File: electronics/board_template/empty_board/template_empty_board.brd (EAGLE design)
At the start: 48 x 48 mm, 8 parts, among them IC1 L7805CD2T-TR, J1 GROVE_CONNECTOR2.0_1X4, J2 GROVE_CONNECTOR2.0_1X4

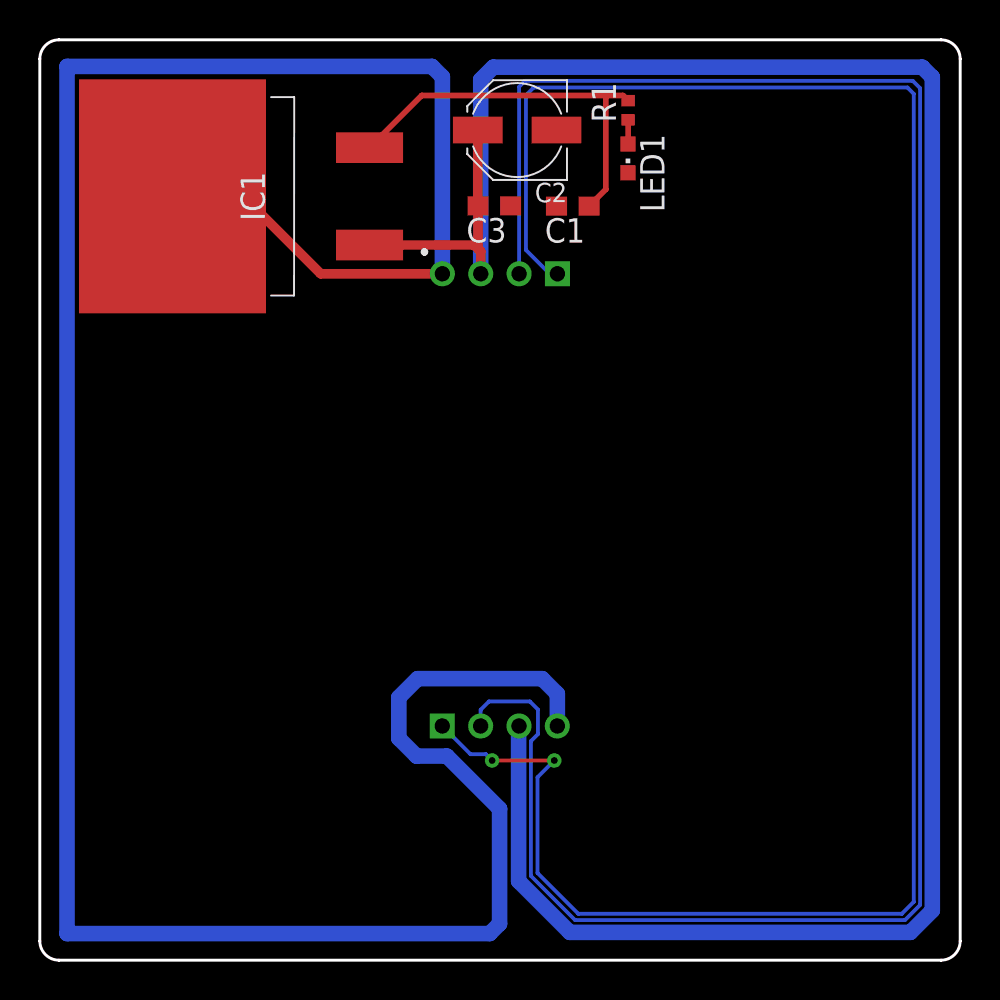
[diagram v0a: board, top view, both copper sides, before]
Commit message: Template Empty Board an anderen Linearregler angepasst
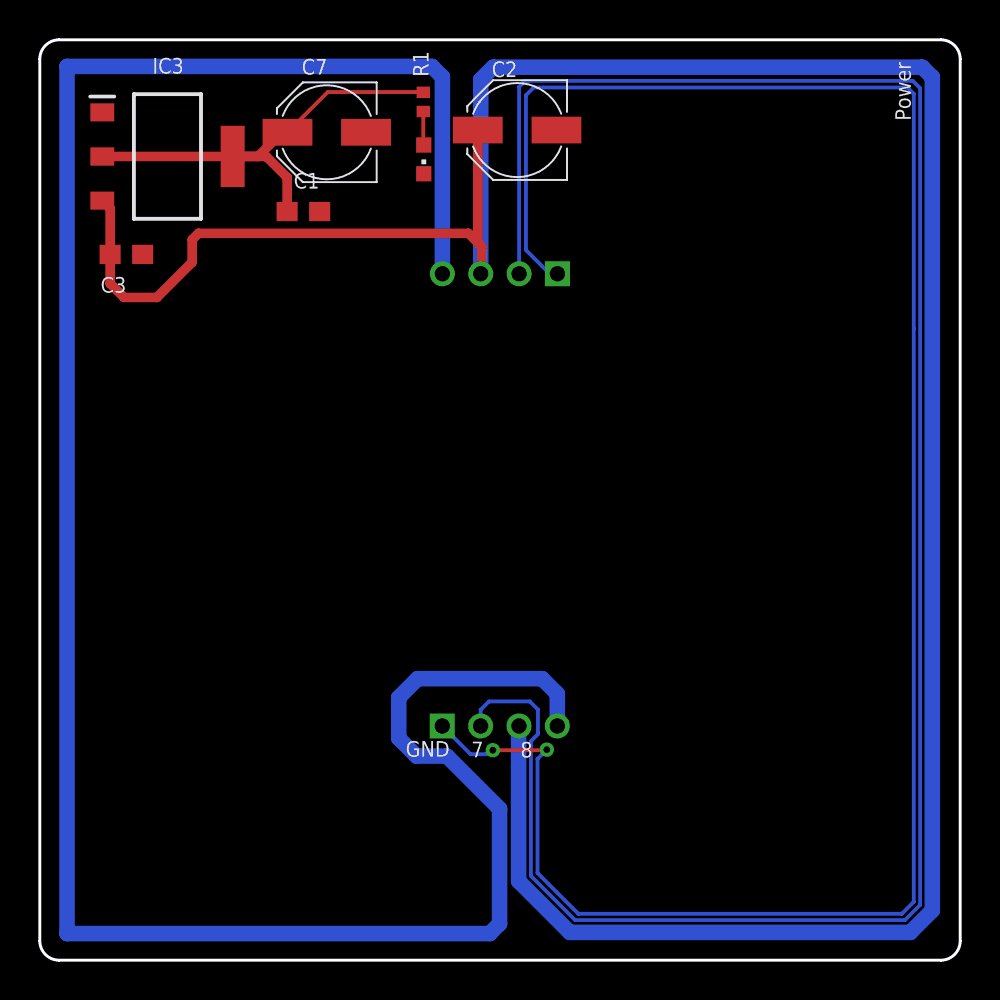
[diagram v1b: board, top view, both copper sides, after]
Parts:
- removed IC1: L7805CD2T-TR, morphbot:L7805CD2T
- added C7: ST(Semtech) CK1C470M-CRD54 - 47uF, rcl:PANASONIC_C
- added IC3: NCP1117ST50T3G, samacsys:SOT230P700X180-4N@1
- moved C3 19.4 mm to (4.52, 36.8)
- moved C1 14.1 mm to (13.7, 39.0), turned to 0 degrees
- moved R1 10.7 mm to (20.0, 44.8)
- moved LED1 10.6 mm to (20.0, 41.8)
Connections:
- net SCL renamed PC5/SCL
- net SDA renamed PC4/SDA
- net +5V: now also C7.+, IC3.2, IC3.4; no longer IC1.3
- net GND: now also C7.-, IC3.1; no longer IC1.2
- net VCC: now also IC3.3; no longer IC1.1
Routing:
- net VCC: track 122.4 -> 143.0 mm
- net GND: track 139.4 -> 124.3 mm
- net +5V: track 20.9 -> 23.9 mm
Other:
- board text added: "7"
- board text added: "8"
- board text added: "GND"
- board text added: "Power"

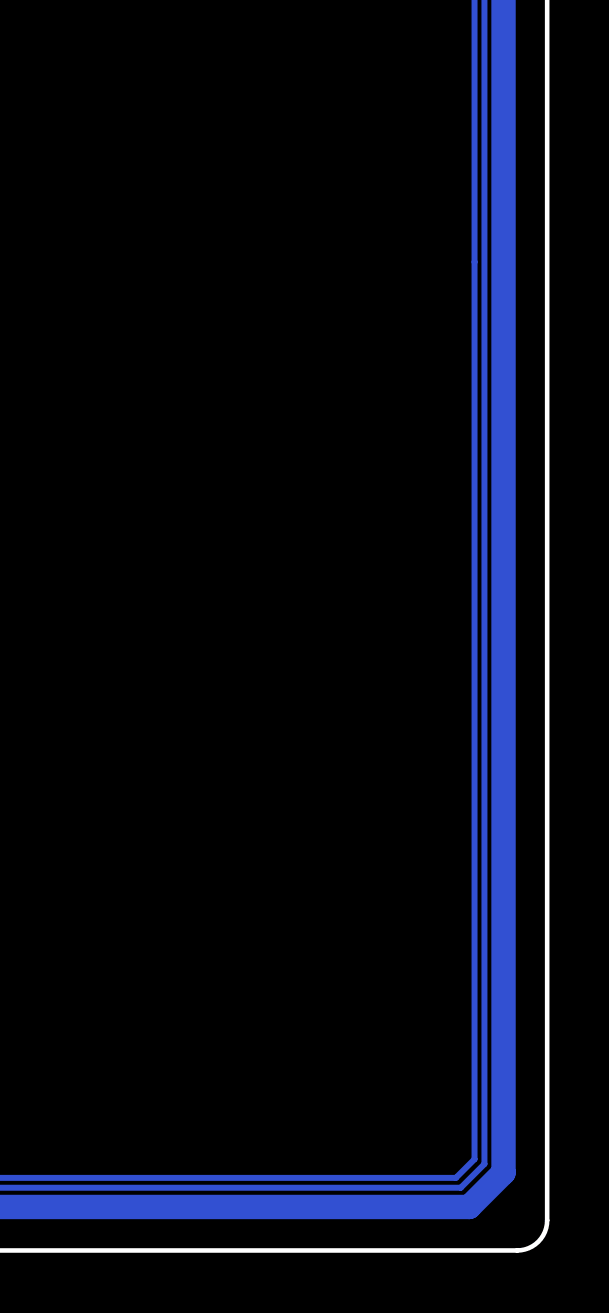
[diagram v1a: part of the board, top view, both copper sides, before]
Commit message: Logo hinzugefügt
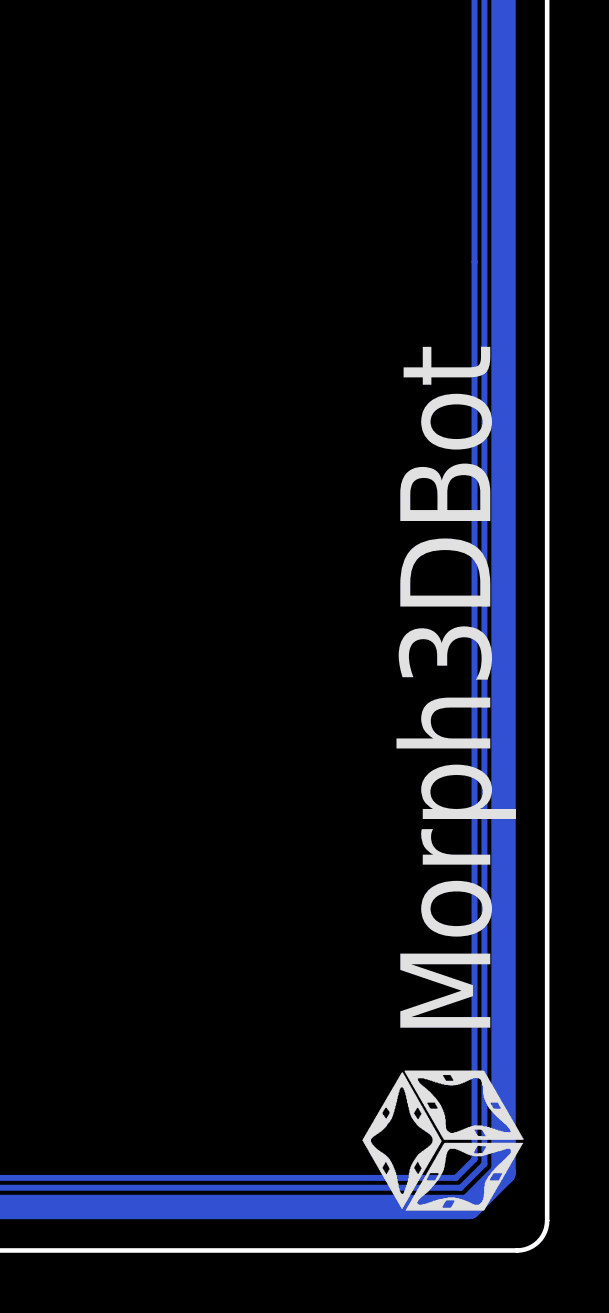
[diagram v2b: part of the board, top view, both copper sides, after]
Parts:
- added U$1: LOGO_MORPHBOT5MM, topo-eng:LOGO_MORPHBOT
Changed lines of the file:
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@@
 <layer number="104" name="Name" color="7" fill="1" visible="no" active="yes"/>
 <layer number="116" name="Patch_BOT" color="9" fill="4" visible="no" active="yes"/>
+<layer number="120" name="brd_placement_notes" color="7" fill="1" visible="yes" active="yes"/>
 <layer number="121" name="_tsilk" color="7" fill="1" visible="no" active="yes"/>
 <layer number="122" name="_bsilk" color="7" fill="1" visible="no" active="yes"/>
+<layer number="144" name="DrillLegend" color="7" fill="1" visible="yes" active="yes"/>
+<layer number="145" name="DrillLegend_01-16" color="7" fill="1" visible="yes" active="yes"/>
+<layer number="146" name="DrillLegend_01-20" color="7" fill="1" visible="yes" active="yes"/>
 <layer number="151" name="HeatSink" color="14" fill="1" visible="no" active="no"/>
+<layer number="198" name="BMP198" color="7" fill="1" visible="yes" active="yes"/>
+<layer number="199" name="Contour" color="7" fill="1" visible="yes" active="yes"/>
 <layer number="200" name="200bmp" color="1" fill="10" visible="no" active="no"/>
 <layer number="201" name="201bmp" color="2" fill="1" visible="no" active="no"/>
@@
 <layer number="207" name="207bmp" color="15" fill="10" visible="no" active="no"/>
 <layer number="208" name="208bmp" color="9" fill="10" visible="no" active="yes"/>
+<layer number="209" name="Route9Document" color="7" fill="1" visible="yes" active="yes"/>
+<layer number="210" name="Route10Document" color="7" fill="1" visible="yes" active="yes"/>
+<layer number="211" name="Route11Document" color="7" fill="1" visible="yes" active="yes"/>
+<layer number="212" name="Route12Document" color="7" fill="1" visible="yes" active="yes"/>
+<layer number="213" name="Route13Document" color="7" fill="1" visible="yes" active="yes"/>
+<layer number="214" name="Route14Document" color="7" fill="1" visible="yes" active="yes"/>
+<layer number="215" name="Route15Document" color="7" fill="1" visible="yes" active="yes"/>
+<layer number="216" name="BottomDocument" color="7" fill="1" visible="yes" active="yes"/>
+<layer number="220" name="DimensionDocument" color="7" fill="1" visible="yes" active="yes"/>
+<layer number="221" name="tPlaceDocument" color="7" fill="1" visible="yes" active="yes"/>
+<layer number="222" name="bPlaceDocument" color="7" fill="1" visible="yes" active="yes"/>
+<layer number="225" name="tNamesDocument" color="7" fill="1" visible="yes" active="yes"/>
+<layer number="226" name="bNamesDocument" color="7" fill="1" visible="yes" active="yes"/>
+<layer number="227" name="tValuesDocument" color="7" fill="1" visible="yes" active="yes"/>
+<layer number="228" name="bValuesDocument" color="7" fill="1" visible="yes" active="yes"/>
+<layer number="229" name="tStopDocument" color="7" fill="1" visible="yes" active="yes"/>
+<layer number="230" name="bStopDocument" color="7" fill="1" visible="yes" active="yes"/>
+<layer number="231" name="tCreamDocument" color="7" fill="1" visible="yes" active="yes"/>
+<layer number="232" name="bCreamDocument" color="7" fill="1" visible="yes" active="yes"/>
+<layer number="233" name="tFinishDocument" color="7" fill="1" visible="yes" active="yes"/>
+<layer number="234" name="bFinishDocument" color="7" fill="1" visible="yes" active="yes"/>
+<layer number="235" name="tGlueDocument" color="7" fill="1" visible="yes" active="yes"/>
+<layer number="236" name="bGlueDocument" color="7" fill="1" visible="yes" active="yes"/>
+<layer number="244" name="DrillsDocument" color="7" fill="1" visible="yes" active="yes"/>
+<layer number="245" name="HolesDocument" color="7" fill="1" visible="yes" active="yes"/>
+<layer number="246" name="MillingDocument" color="7" fill="1" visible="yes" active="yes"/>
+<layer number="247" name="MeasuresDocument" color="7" fill="1" visible="yes" active="yes"/>
 <layer number="250" name="Descript" color="3" fill="1" visible="no" active="no"/>
 <layer number="251" name="SMDround" color="12" fill="11" visible="no" active="no"/>
@@
 <attribute name="VALUE" x="17.61630625" y="46.952225" size="1.016" layer="27" rot="R180"/>
 </element>
+<element name="U$1" library="topo-eng" library_urn="urn:adsk.eagle:library:6646478" package="LOGO_MORPHBOT" value="LOGO_MORPHBOT5MM" x="47.314" y="1.0827625" smashed="yes" rot="R90"/>
 </elements>
 <signals>

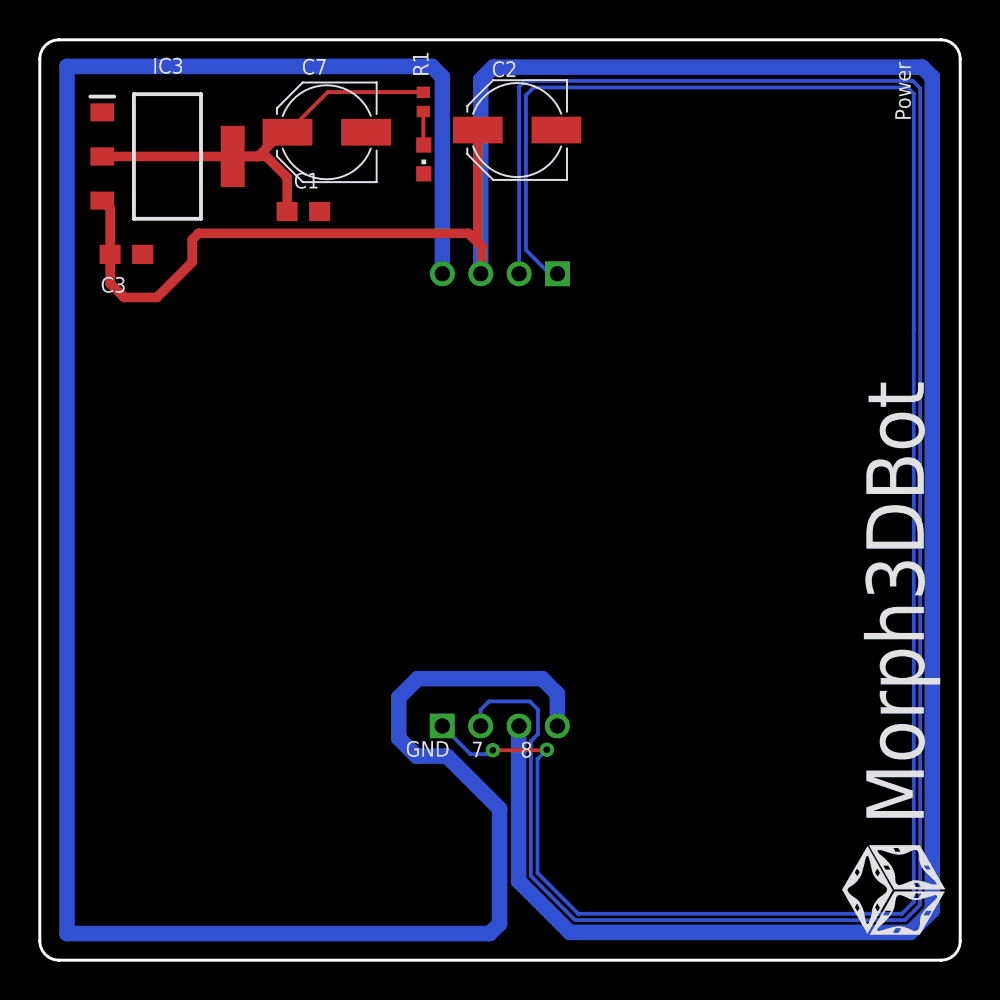
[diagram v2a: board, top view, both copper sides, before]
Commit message: Fiducials eingefügt
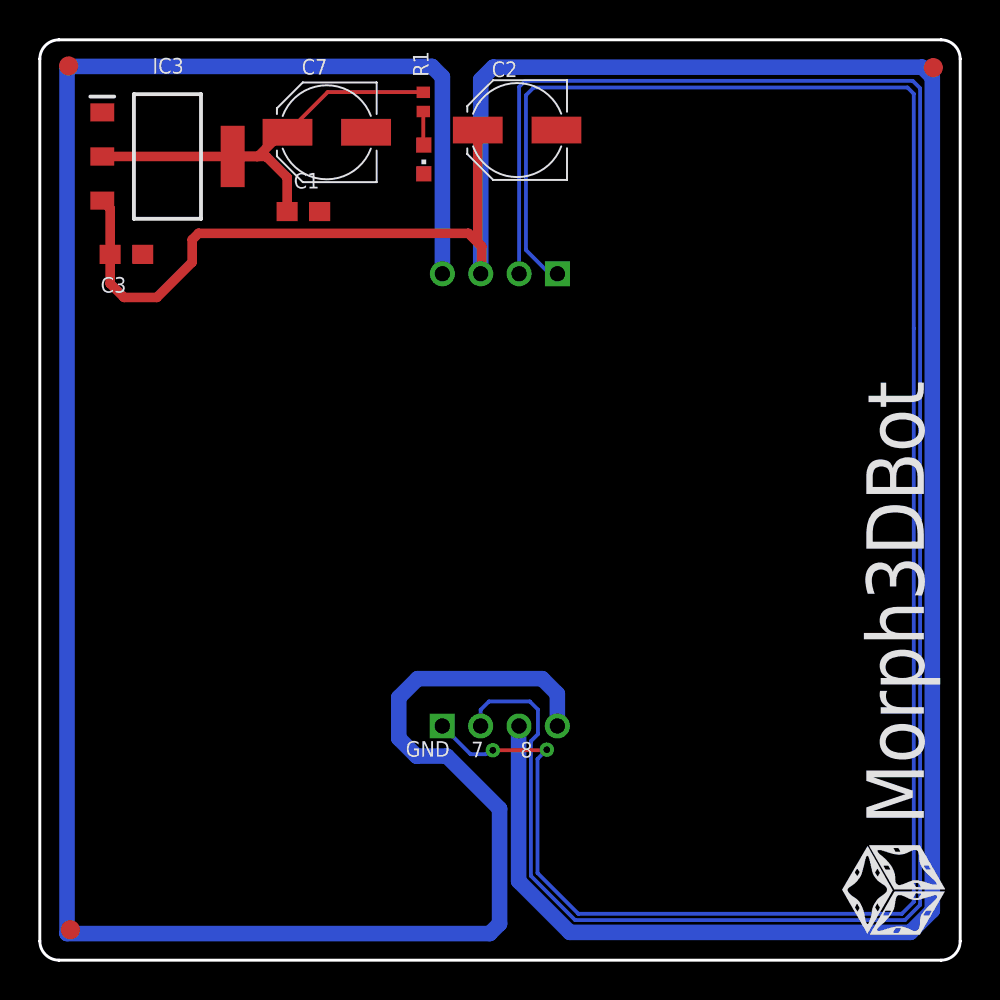
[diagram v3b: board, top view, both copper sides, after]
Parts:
- added FID1, FID2, FID3: OPEN-PNP-FIDUCIAL, topo-eng:OPEN-PNP-FIDUCIAL
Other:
- board text removed: "Power"
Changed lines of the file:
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@@
 <vertex x="24" y="0"/>
 </polygon>
-<text x="45.424440625" y="43.780675" size="0.8128" layer="25" rot="R90">Power</text>
 <text x="19.077415625" y="10.61233125" size="0.8128" layer="25">GND</text>
 <text x="22.5004125" y="10.581159375" size="0.8128" layer="25">7</text>
@@
 </element>
 <element name="U$1" library="topo-eng" library_urn="urn:adsk.eagle:library:6646478" package="LOGO_MORPHBOT" value="LOGO_MORPHBOT5MM" x="47.314" y="1.0827625" smashed="yes" rot="R90"/>
+<element name="FID1" library="topo-eng" library_urn="urn:adsk.eagle:library:6646478" package="OPEN-PNP-FIDUCIAL" value="OPEN-PNP-FIDUCIAL" x="1.59386875" y="1.585840625" smashed="yes"/>
+<element name="FID2" library="topo-eng" library_urn="urn:adsk.eagle:library:6646478" package="OPEN-PNP-FIDUCIAL" value="OPEN-PNP-FIDUCIAL" x="1.50239375" y="46.63590625" smashed="yes"/>
+<element name="FID3" library="topo-eng" library_urn="urn:adsk.eagle:library:6646478" package="OPEN-PNP-FIDUCIAL" value="OPEN-PNP-FIDUCIAL" x="46.599640625" y="46.5495125" smashed="yes"/>
 </elements>
 <signals>
